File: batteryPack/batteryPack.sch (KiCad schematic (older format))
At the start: 38 parts, among them J1 Mirco USB, J10 B1+, J11 B1-, J12 B2-, J13 B1+, J14 B1-, J15 B2+, J16 B2-, J2 B1+, J3 B1-, J4 B2-, J5 B2+, J6 CableConnector, J7 SWD, J8 UART, J9 B2+, P1 USB-C, U1 TP5100-Module, U2 STM32F030F4Px, U3 HT7533-1, U4 TP5100-Module

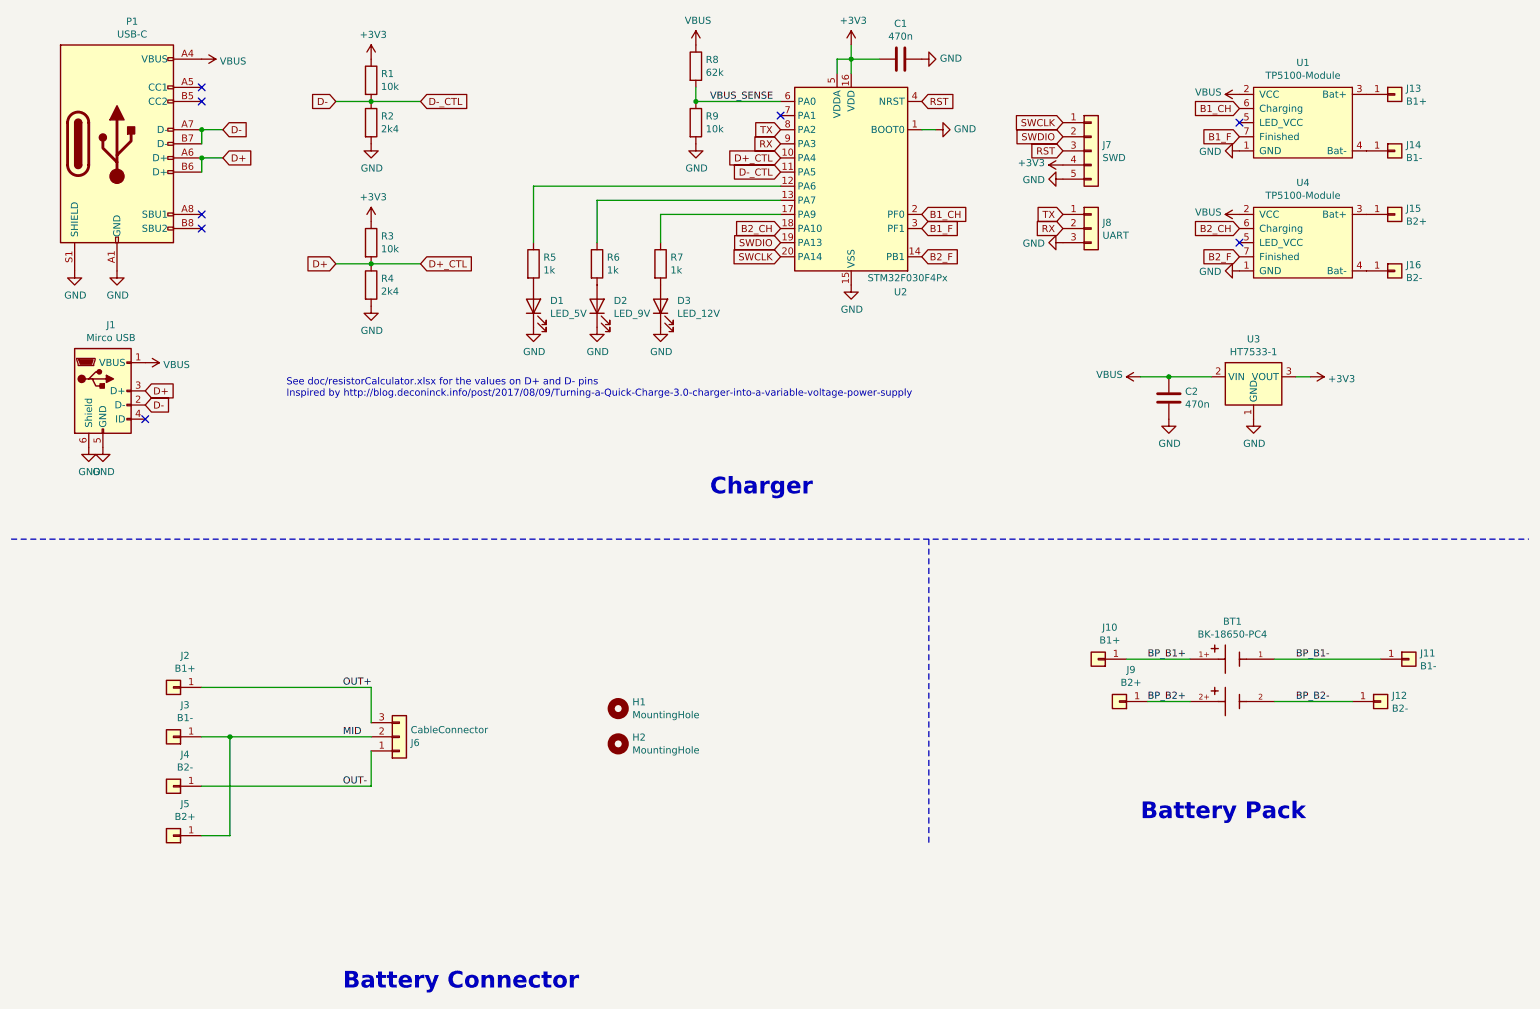
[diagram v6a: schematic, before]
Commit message: Add battery voltage signalization
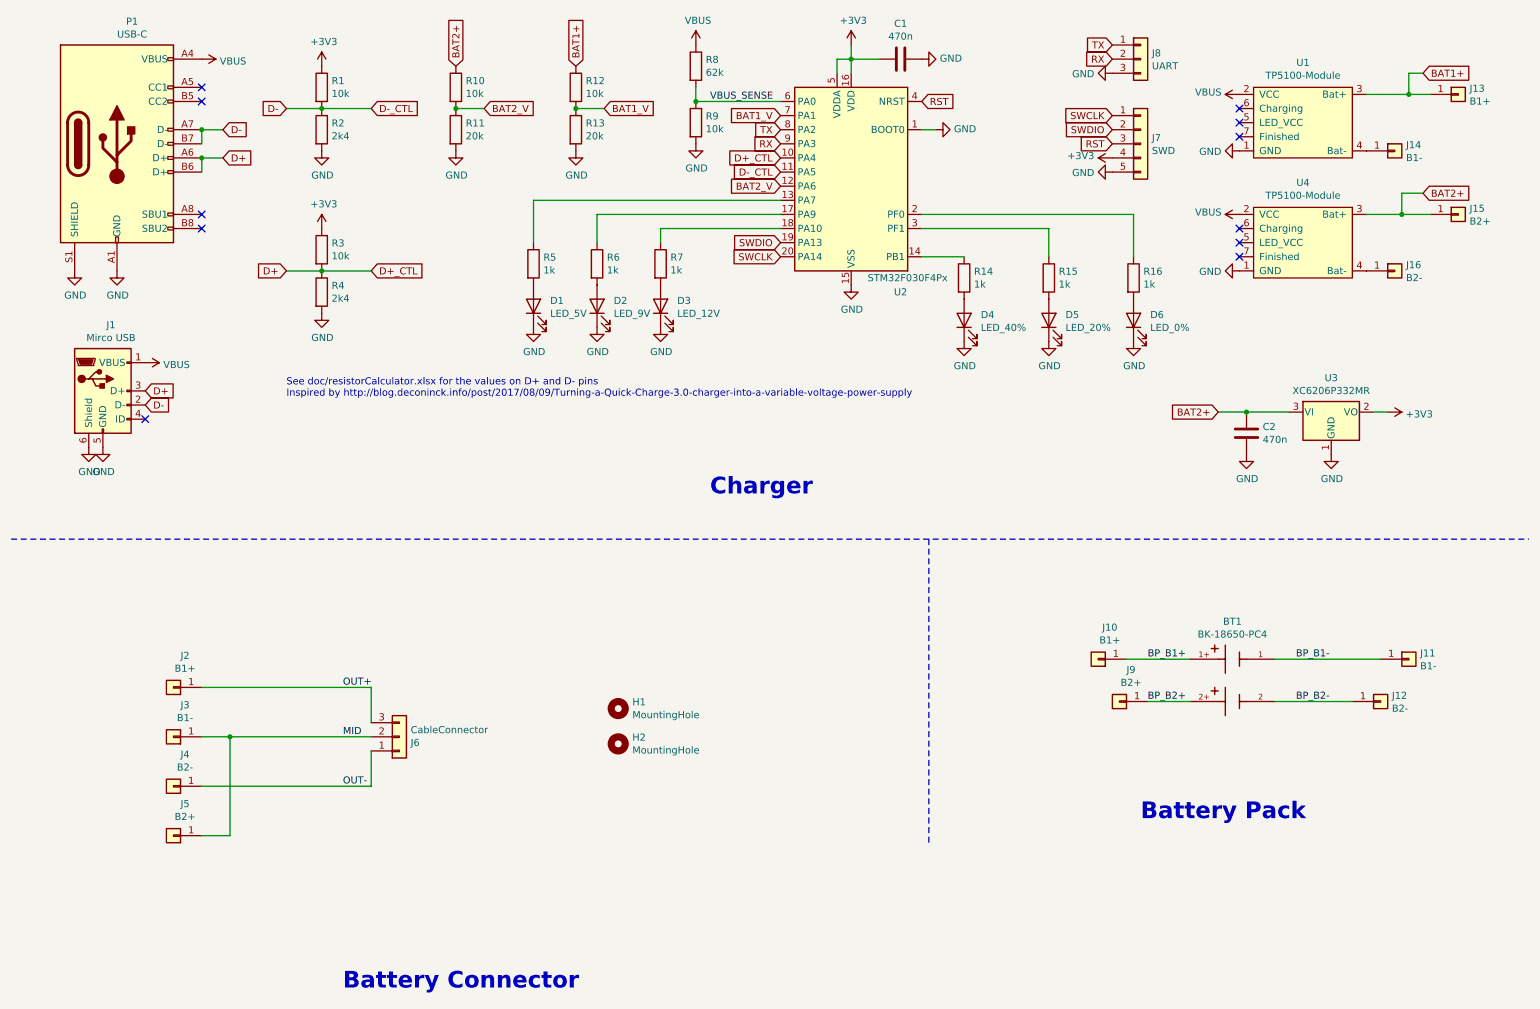
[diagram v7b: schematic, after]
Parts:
- removed U3: HT7533-1, Package_TO_SOT_SMD:SOT-89-3, symbol Regulator_Linear:HT75xx-1-SOT89
- added D4: LED_40%, LED_SMD:LED_0603_1608Metric_Pad1.05x0.95mm_HandSolder, symbol Device:LED
- added D5: LED_20%, LED_SMD:LED_0603_1608Metric_Pad1.05x0.95mm_HandSolder, symbol Device:LED
- added D6: LED_0%, LED_SMD:LED_0603_1608Metric_Pad1.05x0.95mm_HandSolder, symbol Device:LED
- added R10, R12: 10k, Resistor_SMD:R_0603_1608Metric_Pad1.05x0.95mm_HandSolder, symbol Device:R
- added R11, R13: 20k, Resistor_SMD:R_0603_1608Metric_Pad1.05x0.95mm_HandSolder, symbol Device:R
- added R14, R15, R16: 1k, Resistor_SMD:R_0603_1608Metric_Pad1.05x0.95mm_HandSolder, symbol Device:R
- added U3: XC6206P332MR, Package_TO_SOT_SMD:SOT-23, symbol Regulator_Linear:XC6206PxxxMR
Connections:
- net +3V3: now also U3.2 (VO)
- net GND: now also D4.1 (K), D5.1 (K), D6.1 (K), R11.2, R13.2, U3.1 (GND)
- net VBUS: no longer C2.2
- net BAT1+: now reaches J13.1 (Pin_1), U1.3 (Bat+)
- net BAT1+: now also R12.1
- net BAT2+: now reaches J15.1 (Pin_1), U4.3 (Bat+)
- net BAT2+: now also C2.2, R10.1, U3.3 (VI)
- net at R5.1: now also U2.13 (PA7); no longer U2.12 (PA6)
- net at R6.1: now also U2.17 (PA9); no longer U2.13 (PA7)
- net at R7.1: now also U2.18 (PA10); no longer U2.17 (PA9)
- net BAT1_V: now reaches U2.7 (PA1)
- net BAT1_V: now also R12.2, R13.1
- net B1_CH: no longer names the net of U1.6 (Charging)
- net B1_CH: no longer U2.2 (PF0)
- net B1_F: no longer names the net of U1.7 (Finished)
- net B1_F: no longer U2.3 (PF1)
- net B2_CH: no longer names the net of U4.6 (Charging)
- net B2_CH: no longer U2.18 (PA10)
- net B2_F: no longer names the net of U4.7 (Finished)
- net B2_F: no longer U2.14 (PB1)
- new net: R14.1, U2.14 (PB1)
- new net: R16.1, U2.2 (PF0)
- new net: R15.1, U2.3 (PF1)
- new net: D4.2 (A), R14.2
- new net: D5.2 (A), R15.2
- new net: D6.2 (A), R16.2
- new net BAT2_V: R10.2, R11.1, U2.12 (PA6)
- no-connect marks 8 -> 11
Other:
- moved on the sheet: C2, J13, J15, J7, J8, R1, R2, R3, R4
